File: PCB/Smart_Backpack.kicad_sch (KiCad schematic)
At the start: 16 parts, among them SW1 SW_Push, U3 ESP32-PICO-MINI-02-N8R2

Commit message: place and route connectors, add edges
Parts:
- removed H6: MountingHole, MountingHole:MountingHole_3mm, symbol Mechanical:MountingHole
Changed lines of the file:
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@@
-	)
-	(symbol
-		(lib_id "Mechanical:MountingHole")
-		(at 114.3 88.9 0)
-		(unit 1)
-		(exclude_from_sim no)
-		(in_bom no)
-		(on_board yes)
-		(dnp no)
-		(fields_autoplaced yes)
-		(property "Reference" "H6"
-			(at 116.84 87.6299 0)
-			(effects
-				(font
-					(size 1.27 1.27)
-				)
-				(justify left)
-			)
-		)
-		(property "Value" "MountingHole"
-			(at 116.84 90.1699 0)
-			(effects
-				(font
-					(size 1.27 1.27)
-				)
-				(justify left)
-			)
-		)
-		(property "Footprint" "MountingHole:MountingHole_3mm"
-			(at 114.3 88.9 0)
-			(effects
-				(font
-					(size 1.27 1.27)
-				)
-				(hide yes)
-			)
-		)
-		(property "Datasheet" "~"
-			(at 114.3 88.9 0)
-			(effects
-				(font
-					(size 1.27 1.27)
-				)
-				(hide yes)
-			)
-		)
-		(property "Description" "Mounting Hole without connection"
-			(at 114.3 88.9 0)
-			(effects
-				(font
-					(size 1.27 1.27)
-				)
-				(hide yes)
-			)
-		)
-		(instances
-			(project "Smart_Backpack"
-				(path "/38abc652-c887-4ef7-a45f-d93ca7f4b2d6"
-					(reference "H6")
-					(unit 1)
-				)
-			)
-		)
 	)
 	(symbol

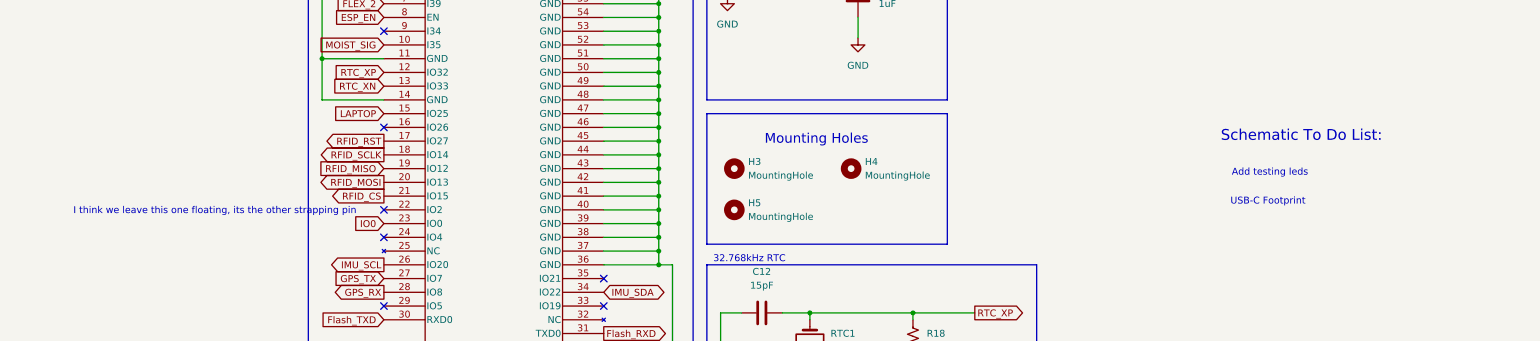
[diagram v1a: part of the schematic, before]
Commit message: Some updates suggested by Ryan (The 1 sem senior design prof)
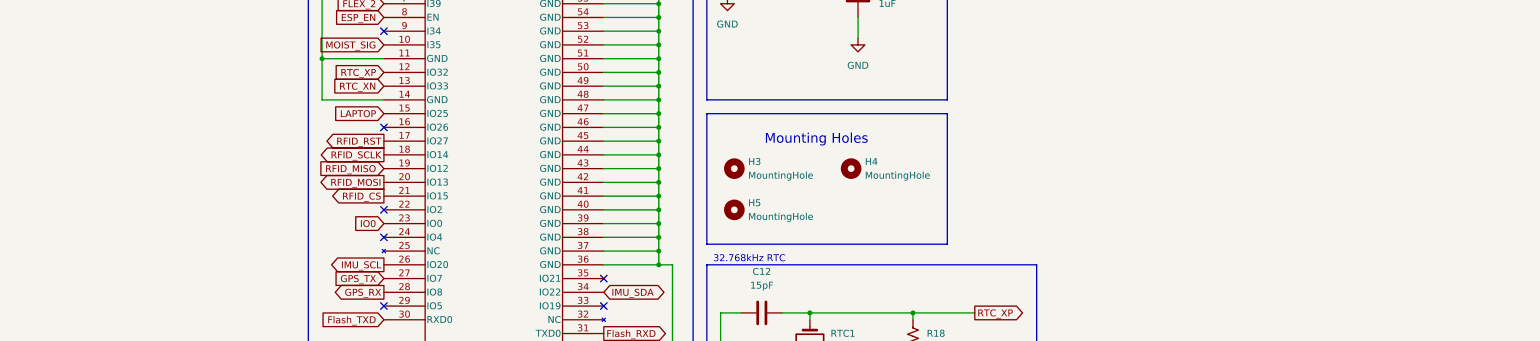
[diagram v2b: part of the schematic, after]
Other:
- note removed: "Add testing leds"
- note removed: "I think we leave this one floating, its the other strapping pin"
- note removed: "Schematic To Do List:"
- note removed: "USB-C Footprint"
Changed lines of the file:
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@@
-		)
-	)
-	(text "USB-C Footprint"
-		(exclude_from_sim no)
-		(at 184.404 88.138 0)
-		(effects
-			(font
-				(size 1.27 1.27)
-			)
-			(justify left bottom)
 		)
 	)
@@
 		(exclude_from_sim no)
 		(at 95.504 98.044 0)
-		(effects
-			(font
-				(size 1.27 1.27)
-			)
-		)
-	)
-	(text "Schematic To Do List:"
-		(exclude_from_sim no)
-		(at 182.626 76.454 0)
-		(effects
-			(font
-				(size 2 2)
-			)
-			(justify left bottom)
-		)
-	)
-	(text "I think we leave this one floating, its the other strapping pin"
-		(exclude_from_sim no)
-		(at -3.302 89.154 0)
 		(effects
 			(font
@@
 			)
 			(justify left bottom)
-		)
-	)
-	(text "Add testing leds"
-		(exclude_from_sim no)
-		(at 184.658 82.804 0)
-		(effects
-			(font
-				(size 1.27 1.27)
-			)
-			(justify left bottom)

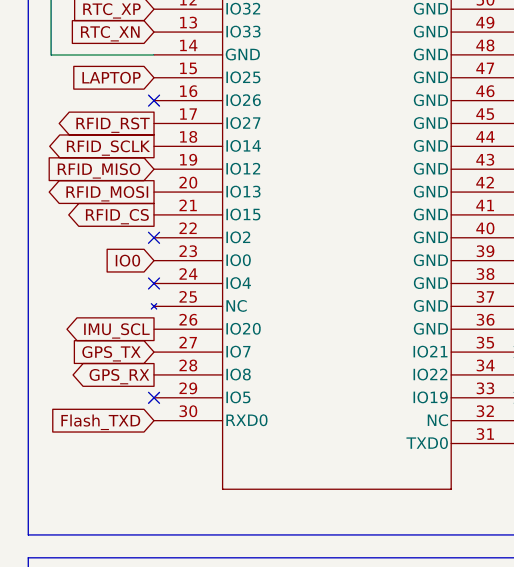
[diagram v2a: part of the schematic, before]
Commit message: Added motors :pensive:
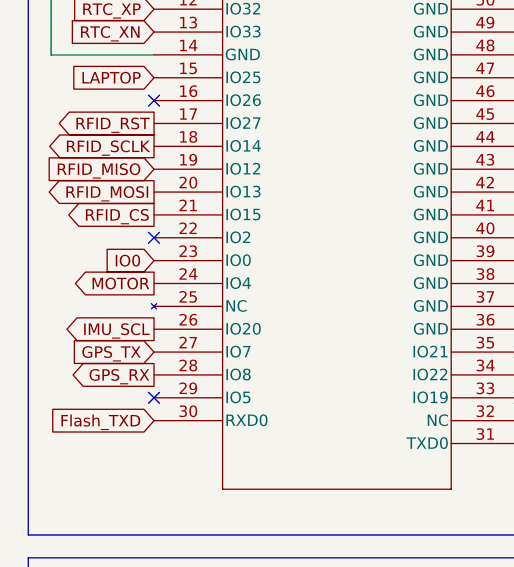
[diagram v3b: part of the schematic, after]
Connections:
- net MOTOR: now reaches U3.24 (IO4)
- no-connect marks 7 -> 6
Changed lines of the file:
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@@
-	)
-	(no_connect
-		(at 27.94 93.98)
 	)
 	(no_connect
@@
 			(effects
 				(font
+					(size 1.27 1.27)
+				)
+				(justify right)
+				(hide yes)
+			)
+		)
+	)
+	(global_label "MOTOR"
+		(shape output)
+		(at 27.94 93.98 180)
+		(fields_autoplaced yes)
+		(effects
+			(font
+				(size 1.27 1.27)
+			)
+			(justify right)
+		)
+		(property "Intersheetrefs" "${INTERSHEET_REFS}"
+			(at 18.6048 93.98 0)
+			(effects
+				(font

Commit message: Alert: Fat inductor incoming
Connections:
- net IMU_INT: now reaches U3.29 (IO5)
- no-connect marks 6 -> 5
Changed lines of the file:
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@@
-	)
-	(no_connect
-		(at 27.94 106.68)
 	)
 	(no_connect
@@
 				(hide yes)
 			)
+		)
+	)
+	(global_label "IMU_INT"
+		(shape output)
+		(at 27.94 106.68 180)
+		(fields_autoplaced yes)
+		(effects
+			(font
+				(size 1.27 1.27)
+			)
+			(justify right)
+		)
+		(property "Intersheetrefs" "${INTERSHEET_REFS}"
+			(at 17.6976 106.68 0)
+			(effects
+				(font
+					(size 1.27 1.27)
+				)
+				(justify right)
+				(hide yes)
+			)

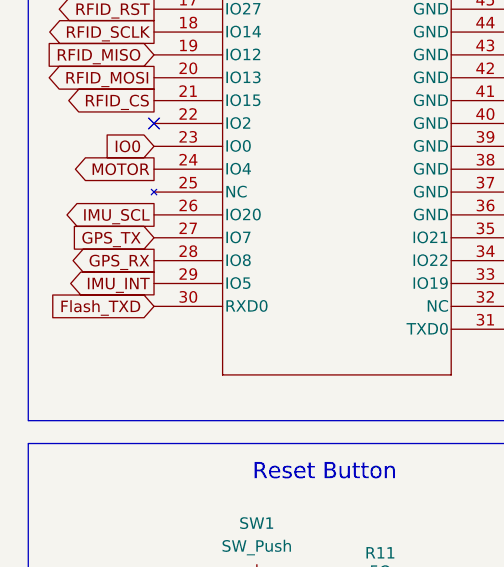
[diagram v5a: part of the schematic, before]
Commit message: fix edge cuts and route IMU_INT
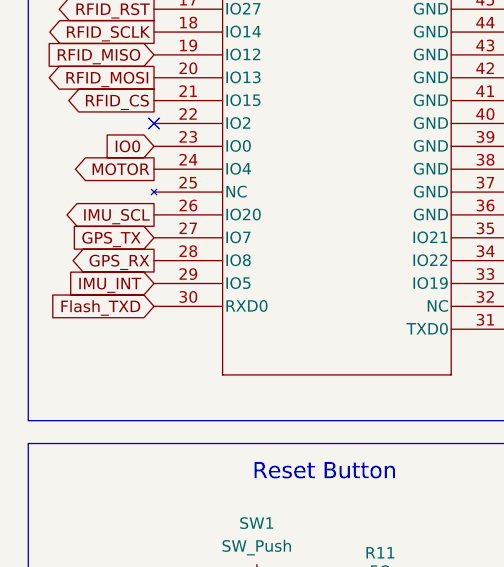
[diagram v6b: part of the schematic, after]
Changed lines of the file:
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@@
 	)
 	(global_label "IMU_INT"
-		(shape output)
+		(shape input)
 		(at 27.94 106.68 180)
 		(fields_autoplaced yes)

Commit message: Start of feedback implementation
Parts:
- added C10, C11: 0.1uF, Capacitor_SMD:C_1206_3216Metric_Pad1.33x1.80mm_HandSolder, symbol Device:C
- added R14: 47.5kΩ, Resistor_SMD:R_1206_3216Metric_Pad1.30x1.75mm_HandSolder, symbol Device:R_US
- added R16: 10kΩ, Resistor_SMD:R_1206_3216Metric_Pad1.30x1.75mm_HandSolder, symbol Device:R_US
- added R17: 5Ω, Resistor_SMD:R_1206_3216Metric_Pad1.30x1.75mm_HandSolder, symbol Device:R_US
- added R2: 2kΩ, Resistor_SMD:R_1206_3216Metric_Pad1.30x1.75mm_HandSolder, symbol Device:R_US
- added R3: 22.1kΩ, Resistor_SMD:R_1206_3216Metric_Pad1.30x1.75mm_HandSolder, symbol Device:R_US
- added SW2: SW_Push, SMD_Button:Shop_SMD_Button, symbol Switch:SW_Push
- added U4: CP2102N-Axx-xQFN28, Package_DFN_QFN:QFN-28-1EP_5x5mm_P0.5mm_EP3.35x3.35mm, symbol Interface_USB:CP2102N-Axx-xQFN28
- R11: value 5Ω -> 0Ω
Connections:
- net +3V3: now also C10.1, R2.1
- net Flash_RXD: now also U4.25 (RXD)
- net Flash_TXD: now also U4.26 (TXD)
- net GND: now also U3.22 (IO2), C11.2, R14.1, R16.2, SW2.1, U4.23 (~{CTS}), U4.29 (GND), U4.3 (GND)
- net IO0: now also R17.2
- new net: C11.1, R17.1, SW2.2
- new net: R16.1, U4.11 (~{SUSPEND})
- new net: C10.2, U4.6 (VDD), U4.7 (VREGIN)
- new net: R14.2, R3.1, U4.8 (VBUS)
- new net: R2.2, U4.9 (~{RST})
- new net +5V: R3.2
- new net DRT: U4.28 (~{DTR})
- new net RTS: U4.24 (~{RTS})
- new net USB_D+: U4.4 (D+)
- new net USB_D-: U4.5 (D-)
- no-connect marks 5 -> 18
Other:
- note added: "Flashing hardware"

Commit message: This time for sure...
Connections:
- net RTC_XN: now also U3.12 (IO32); no longer U3.13 (IO33)
- net RTC_XP: now also U3.13 (IO33); no longer U3.12 (IO32)
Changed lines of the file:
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@@
 	(global_label "RTC_XP"
 		(shape input)
-		(at 27.94 63.5 180)
-		(fields_autoplaced yes)
-		(effects
-			(font
-				(size 1.27 1.27)
-			)
-			(justify right)
-		)
-		(property "Intersheetrefs" "${INTERSHEET_REFS}"
-			(at 18.0001 63.5 0)
+		(at 27.94 66.04 180)
+		(fields_autoplaced yes)
+		(effects
+			(font
+				(size 1.27 1.27)
+			)
+			(justify right)
+		)
+		(property "Intersheetrefs" "${INTERSHEET_REFS}"
+			(at 17.9396 66.04 0)
 			(effects
 				(font
@@
 	(global_label "RTC_XN"
 		(shape input)
-		(at 27.94 66.04 180)
-		(fields_autoplaced yes)
-		(effects
-			(font
-				(size 1.27 1.27)
-			)
-			(justify right)
-		)
-		(property "Intersheetrefs" "${INTERSHEET_REFS}"
-			(at 17.9396 66.04 0)
-			(effects
-				(font
+		(at 27.94 63.5 180)
+		(fields_autoplaced yes)
+		(effects
+			(font
+				(size 1.27 1.27)
+			)
+			(justify right)
+		)
+		(property "Intersheetrefs" "${INTERSHEET_REFS}"
+			(at 18.0001 63.5 0)
+			(effects
+				(font
